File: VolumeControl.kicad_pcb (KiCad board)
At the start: 2 copper layers, 66.5 x 52.1 mm, 42 parts, among them J1 Input R/GND/L, J2 SPI, J3 Screw_Terminal_01x03, J4 5V Supply, J5 Lout, J6 Rout, J7 SubOut, U1 AD5290, U2 AD5290, U3 TL082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

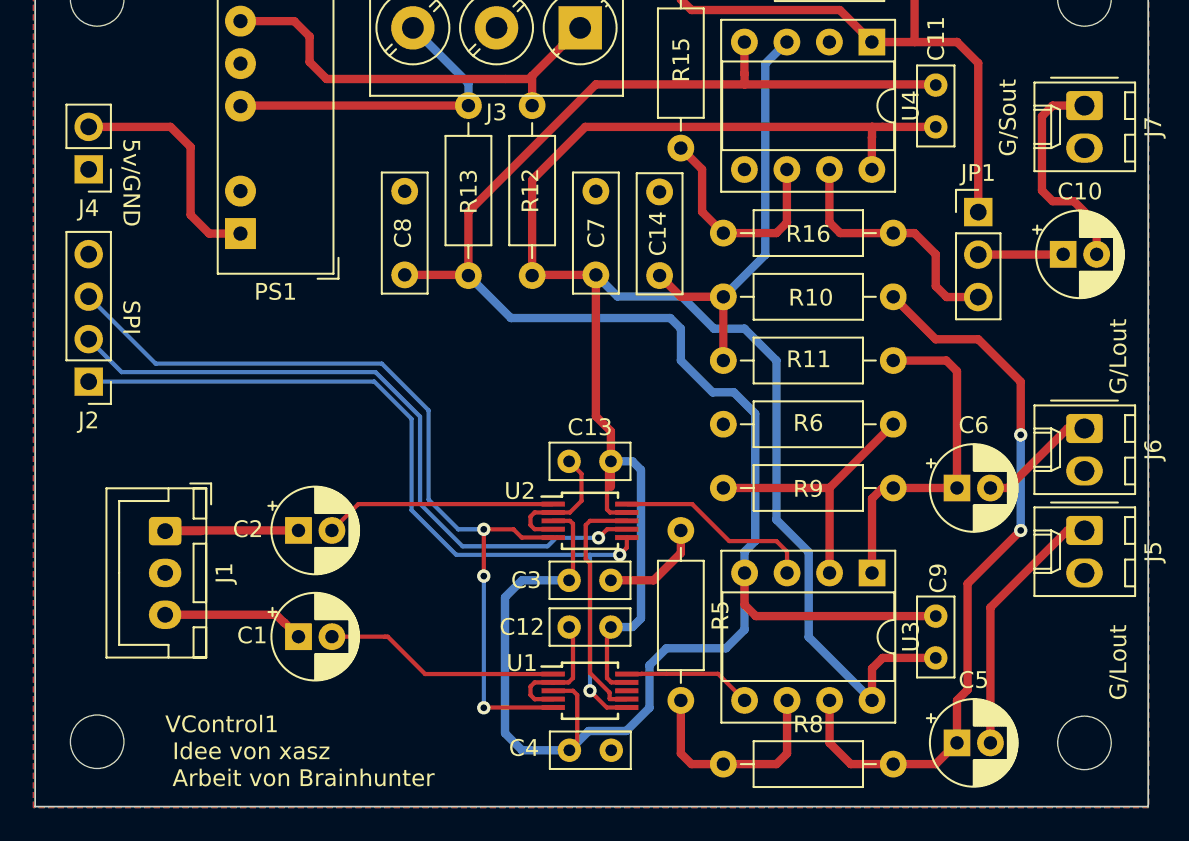
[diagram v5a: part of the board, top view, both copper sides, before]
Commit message: added bypass relais
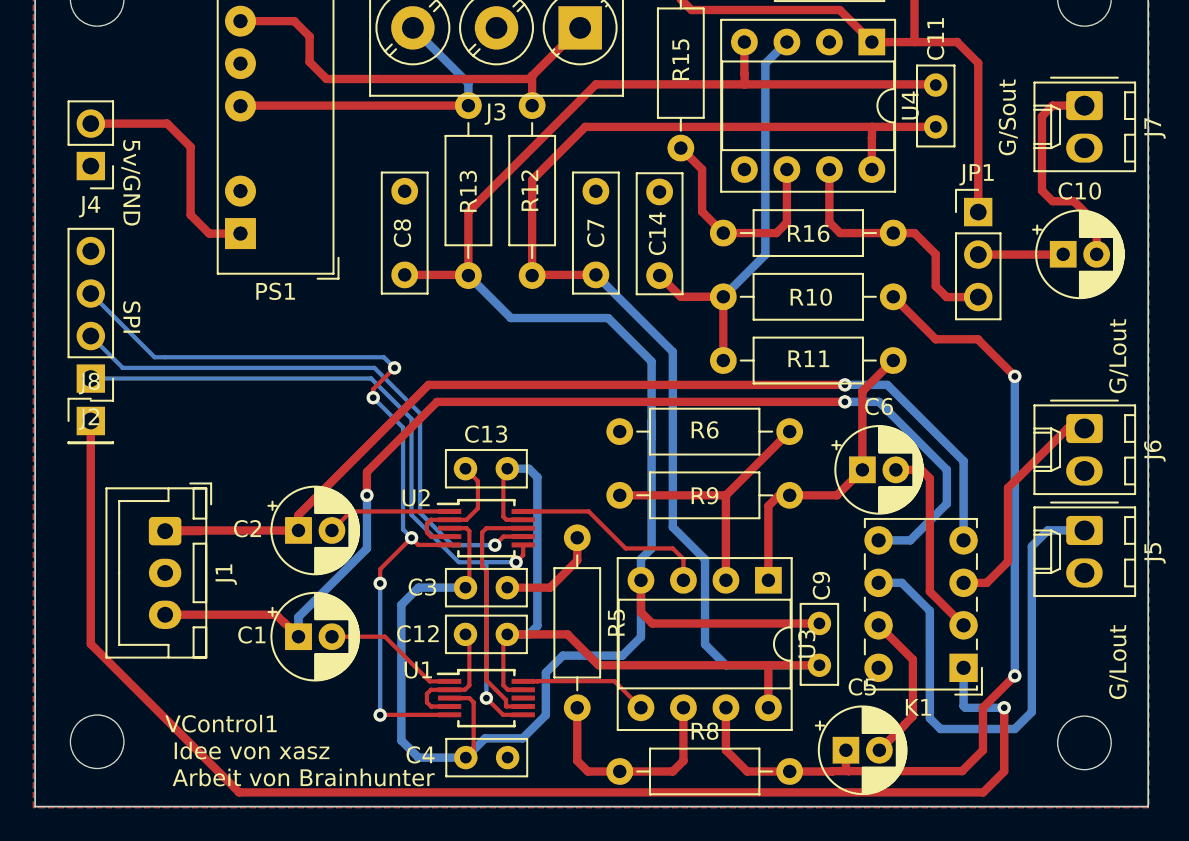
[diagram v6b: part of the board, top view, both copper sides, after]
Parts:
- added J8: Bypass, Connector_PinHeader_2.54mm:PinHeader_1x01_P2.54mm_Vertical, F.Cu at (28.6, 43.8)
- added K1: G6K-2, Relay_THT:Relay_DPDT_Omron_G6K-2P, F.Cu at (80.8, 58.6)
- moved C9 6.97 mm to (72.1, 58.4)
- moved C5 6.66 mm to (73.7, 63.5)
- moved U3 6.21 mm to (69.1, 53.3)
- moved C12 6.21 mm to (53.5, 56.6)
- moved C13 6.21 mm to (53.5, 46.7)
- moved C3 6.21 mm to (53.5, 53.8)
- moved U1 6.21 mm to (52.2, 60.4)
- moved U2 6.21 mm to (52.2, 50.2)
- moved R6 6.21 mm to (60.2, 44.5)
- moved C4 6.21 mm to (53.5, 63.9)
- moved R5 6.21 mm to (57.7, 50.8)
- moved R8 6.21 mm to (60.2, 64.8)
- moved R9 6.21 mm to (60.2, 48.3)
- moved C6 5.76 mm to (74.7, 46.7)
- moved J4 0.23 mm to (28.6, 28.6)
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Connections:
- C5 pad 2: Net-(C5-Pad2) -> PaOutL
- C6 pad 2: Net-(C6-Pad2) -> PaOutR
- J5 pad 1: Net-(C5-Pad2) -> Net-(J5-Pad1)
- J6 pad 1: Net-(C6-Pad2) -> Net-(J6-Pad1)
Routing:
- net Bypass-Relais: track 0.00 -> 80.7 mm, vias 0 -> 1
- net Net-(J1-Pad3): track 8.51 -> 65.2 mm, vias 0 -> 2
- net Net-(C2-Pad1): track 10.1 -> 60.7 mm, vias 0 -> 1
- net Net-(J5-Pad1): track 0.00 -> 30.4 mm
- net Net-(C5-Pad2): track 15.6 -> 0.00 mm
- net Net-(J6-Pad1): track 0.00 -> 13.6 mm
- net PaOutR: track 0.00 -> 11.9 mm
- net PaOutL: track 0.00 -> 9.15 mm
- net Net-(C5-Pad1): track 44.1 -> 52.7 mm
- net Net-(C6-Pad2): track 7.09 -> 0.00 mm
- net Net-(C2-Pad2): track 13.9 -> 7.50 mm
- net /SDI: track 40.8 -> 34.7 mm
- net Net-(U1-Pad1): track 14.2 -> 8.14 mm
- net /CLK: track 51.2 -> 45.6 mm
- net -12VA: track 131.1 -> 126.4 mm
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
